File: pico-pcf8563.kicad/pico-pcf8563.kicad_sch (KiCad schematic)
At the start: 13 parts, among them J1 Stemma-QT_Qwicc, J2 Ext_Conn, J4 Pico Pin 1-7, J5 Pico Pin 40-34, U1 PCF8563T, Y1 Crystal

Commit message: Rev2
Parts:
- removed JP1: VDD_SEL, Jumper:SolderJumper-3_P1.3mm_Bridged12_Pad1.0x1.5mm, symbol Jumper:Jumper_3_Bridged12
- added JP1: 3V3_Jumper, Jumper:SolderJumper-2_P1.3mm_Bridged_Pad1.0x1.5mm, symbol Jumper:Jumper_2_Bridged
- added JP2: ~{INT}_Jumper, Jumper:SolderJumper-2_P1.3mm_Bridged_Pad1.0x1.5mm, symbol Jumper:Jumper_2_Bridged
- added JP3: COUT_Jumper, Jumper:SolderJumper-2_P1.3mm_Bridged_Pad1.0x1.5mm, symbol Jumper:Jumper_2_Bridged
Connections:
- net VDD is gone; now on net VCC: C1.1, R2.2, R3.2, U1.8 (VDD)
- net +3V3: now also JP1.1 (A)
- net COUT: now also JP2.2 (B)
- net VCC: now also JP1.2 (B)
- net ~{INT}: now also JP3.2 (B)
- net GP4: now reaches J4.6 (Pin_6)
- net GP4: now also JP2.1 (A)
- net GP5: now reaches J4.7 (Pin_7)
- net GP5: now also JP3.1 (A)
- no-connect marks 9 -> 7

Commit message: Rev 3
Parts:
- JP2: value ~{INT}_Jumper -> COUT_Jumper
- JP3: value COUT_Jumper -> ~{INT}_Jumper
- R2: value 100K -> 10K; LCSC C25741 -> C25744
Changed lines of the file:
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@@
   (title_block
     (title "pico-pcf8563")
-    (date "2023-01-23")
-    (rev "2")
+    (date "2023-01-27")
+    (rev "3")
     (company "Bernhard Bablok")
     (comment 1 "https://github.com/bablokb/pcb-pico-pcf8563")
@@
     (in_bom yes) (on_board yes)
     (property "Reference" "JP3" (id 0) (at 123.19 150.495 0))
-    (property "Value" "COUT_Jumper" (id 1) (at 123.19 153.035 0))
+    (property "Value" "~{INT}_Jumper" (id 1) (at 123.19 153.035 0))
     (property "Footprint" "Jumper:SolderJumper-2_P1.3mm_Bridged_Pad1.0x1.5mm" (id 2) (at 123.19 155.575 0)
       (effects (font (size 1.27 1.27)) hide)
@@
       (effects (font (size 1.27 1.27)) (justify left))
     )
-    (property "Value" "100K" (id 1) (at 113.665 82.55 90)
-      (effects (font (size 0.9 0.9)) (justify left))
+    (property "Value" "10K" (id 1) (at 113.665 82.55 90)
+      (effects (font (size 1.27 1.27)) (justify left))
     )
     (property "Footprint" "Resistor_SMD:R_0402_1005Metric" (id 2) (at 115.57 80.772 90)
@@
       (effects (font (size 1.27 1.27)) hide)
     )
-    (property "LCSC" "C25741" (id 4) (at 115.57 82.55 0)
+    (property "LCSC" "C25744" (id 4) (at 115.57 82.55 0)
       (effects (font (size 1.27 1.27)) hide)
     )
@@
     (in_bom yes) (on_board yes)
     (property "Reference" "JP2" (id 0) (at 123.19 141.605 0))
-    (property "Value" "~{INT}_Jumper" (id 1) (at 123.19 144.145 0))
+    (property "Value" "COUT_Jumper" (id 1) (at 123.19 144.145 0))
     (property "Footprint" "Jumper:SolderJumper-2_P1.3mm_Bridged_Pad1.0x1.5mm" (id 2) (at 123.19 146.685 0)
       (effects (font (size 1.27 1.27)) hide)
@@
     )
     (path "/bec03931-09e6-4e41-b61c-87083fe69a87"
-      (reference "JP2") (unit 1) (value "~{INT}_Jumper") (footprint "Jumper:SolderJumper-2_P1.3mm_Bridged_Pad1.0x1.5mm")
+      (reference "JP2") (unit 1) (value "COUT_Jumper") (footprint "Jumper:SolderJumper-2_P1.3mm_Bridged_Pad1.0x1.5mm")
     )
     (path "/3c208f7b-fcc2-486a-9f3a-6889a08b4663"
-      (reference "JP3") (unit 1) (value "COUT_Jumper") (footprint "Jumper:SolderJumper-2_P1.3mm_Bridged_Pad1.0x1.5mm")
+      (reference "JP3") (unit 1) (value "~{INT}_Jumper") (footprint "Jumper:SolderJumper-2_P1.3mm_Bridged_Pad1.0x1.5mm")
     )
     (path "/bb0b989e-b5a1-46a4-90cb-50f164e6ade9"
@@
     )
     (path "/b8429782-e8d6-4c46-a9d4-176962d20a7f"
-      (reference "R2") (unit 1) (value "100K") (footprint "Resistor_SMD:R_0402_1005Metric")
+      (reference "R2") (unit 1) (value "10K") (footprint "Resistor_SMD:R_0402_1005Metric")
     )
     (path "/23a3edd9-37fe-4f82-bb93-ec19c92c0a0d"

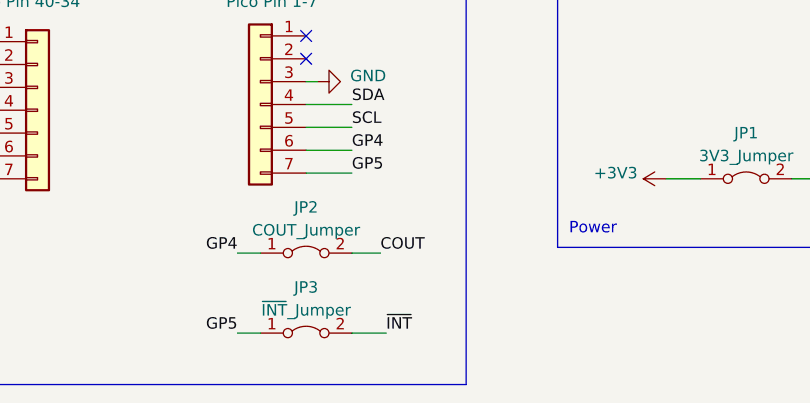
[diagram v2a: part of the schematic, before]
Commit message: Rev 4: swapped INT/CLKOUT. The latter is now on GP5
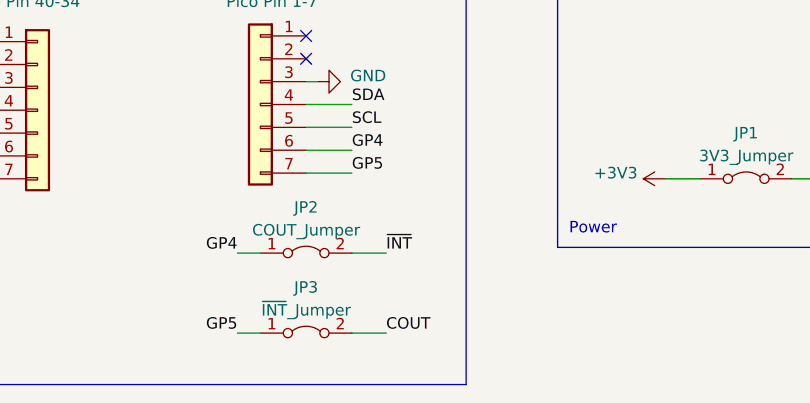
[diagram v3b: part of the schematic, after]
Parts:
- J1, J2, J4, J5, JP1, JP2, JP3: now left out of the parts list
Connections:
- net COUT: now also JP3.2 (B); no longer JP2.2 (B)
- net ~{INT}: now also JP2.2 (B); no longer JP3.2 (B)
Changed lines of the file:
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@@
   (title_block
     (title "pico-pcf8563")
-    (date "2023-01-27")
-    (rev "3")
+    (date "2023-03-08")
+    (rev "4")
     (company "Bernhard Bablok")
     (comment 1 "https://github.com/bablokb/pcb-pico-pcf8563")
@@
     (stroke (width 0) (type default) (color 0 0 0 0))
   )
-  (wire (pts (xy 132.08 155.575) (xy 128.27 155.575))
-    (stroke (width 0) (type default) (color 0 0 0 0))
-  )
   (wire (pts (xy 93.98 55.88) (xy 98.425 55.88))
     (stroke (width 0) (type default) (color 0 0 0 0))
@@
     (stroke (width 0) (type default) (color 0 0 0 0))
   )
+  (wire (pts (xy 128.27 146.685) (xy 132.08 146.685))
+    (stroke (width 0) (type default) (color 0 0 0 0))
+  )
   (wire (pts (xy 101.6 50.8) (xy 111.76 50.8))
     (stroke (width 0) (type default) (color 0 0 0 0))
@@
     (stroke (width 0) (type default) (color 0 0 0 0))
   )
-  (wire (pts (xy 131.445 146.685) (xy 128.27 146.685))
-    (stroke (width 0) (type default) (color 0 0 0 0))
-  )
   (wire (pts (xy 98.425 90.805) (xy 93.345 90.805))
+    (stroke (width 0) (type default) (color 0 0 0 0))
+  )
+  (wire (pts (xy 128.27 155.575) (xy 132.08 155.575))
     (stroke (width 0) (type default) (color 0 0 0 0))
   )
@@
     (effects (font (size 1.27 1.27)) (justify left bottom))
   )
-  (label "COUT" (at 131.445 146.685 0)
+  (label "COUT" (at 132.08 155.575 0)
     (effects (font (size 1.27 1.27)) (justify left bottom))
   )
@@
     (effects (font (size 1.27 1.27)) (justify right bottom))
   )
-  (label "~{INT}" (at 132.08 155.575 0)
+  (label "~{INT}" (at 132.08 146.685 0)
     (effects (font (size 1.27 1.27)) (justify left bottom))
   )
@@
   )
   (symbol (lib_id "Connector_Generic:Conn_01x06") (at 205.74 64.77 0) (unit 1)
-    (in_bom yes) (on_board yes)
+    (in_bom no) (on_board yes)
     (property "Reference" "J2" (id 0) (at 203.835 51.435 0)
       (effects (font (size 1.27 1.27)) (justify left))
@@
   )
   (symbol (lib_id "Jumper:Jumper_2_Bridged") (at 123.19 155.575 0) (unit 1)
-    (in_bom yes) (on_board yes)
+    (in_bom no) (on_board yes)
     (property "Reference" "JP3" (id 0) (at 123.19 150.495 0))
     (property "Value" "~{INT}_Jumper" (id 1) (at 123.19 153.035 0))
@@
   )
   (symbol (lib_id "Connector_Generic:Conn_01x07") (at 93.345 130.81 0) (unit 1)
-    (in_bom yes) (on_board yes)
+    (in_bom no) (on_board yes)
     (property "Reference" "J5" (id 0) (at 92.075 114.935 0)
       (effects (font (size 1.27 1.27)) (justify left))
@@
   )
   (symbol (lib_id "Connector_Generic:Conn_01x07") (at 118.11 130.175 0) (mirror y) (unit 1)
-    (in_bom yes) (on_board yes)
+    (in_bom no) (on_board yes)
     (property "Reference" "J4" (id 0) (at 119.38 115.57 0)
       (effects (font (size 1.27 1.27)) (justify left))
@@
   )
   (symbol (lib_id "Jumper:Jumper_2_Bridged") (at 172.085 138.43 0) (unit 1)
-    (in_bom yes) (on_board yes)
+    (in_bom no) (on_board yes)
     (property "Reference" "JP1" (id 0) (at 172.085 133.35 0))
     (property "Value" "3V3_Jumper" (id 1) (at 172.085 135.89 0))
@@
   )
   (symbol (lib_id "user:Stemma-QT_Qwicc") (at 169.545 62.865 0) (unit 1)
-    (in_bom yes) (on_board yes)
+    (in_bom no) (on_board yes)
     (property "Reference" "J1" (id 0) (at 169.545 50.8 0)
       (effects (font (size 1.27 1.27)) (justify left))
@@
   )
   (symbol (lib_id "Jumper:Jumper_2_Bridged") (at 123.19 146.685 0) (unit 1)
-    (in_bom yes) (on_board yes)
+    (in_bom no) (on_board yes)
     (property "Reference" "JP2" (id 0) (at 123.19 141.605 0))
     (property "Value" "COUT_Jumper" (id 1) (at 123.19 144.145 0))
@@
       (effects (font (size 1.27 1.27)) hide)
     )
-    (property "Datasheet" "https://assets.nexperia.com/documents/data-sheet/PCF8563.pdf" (id 3) (at 111.76 60.96 0)
-      (effects (font (size 1.27 1.27)) hide)
-    )
+    (property "Datasheet" "https://www.nxp.com/docs/en/data-sheet/PCF8563.pdf" (id 3) (at 111.76 60.96 0)
+      (effects (font (size 1.27 1.27)) hide)
+    )
